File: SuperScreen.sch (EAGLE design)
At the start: 30 parts, among them CN1 AMP FCI 10103594-0001LF, CN2 JSTPH, CN3 1X4-BIG, IC2 MIC5225, Q3 BSS138, U2 MCP73831T-2ACI/OT

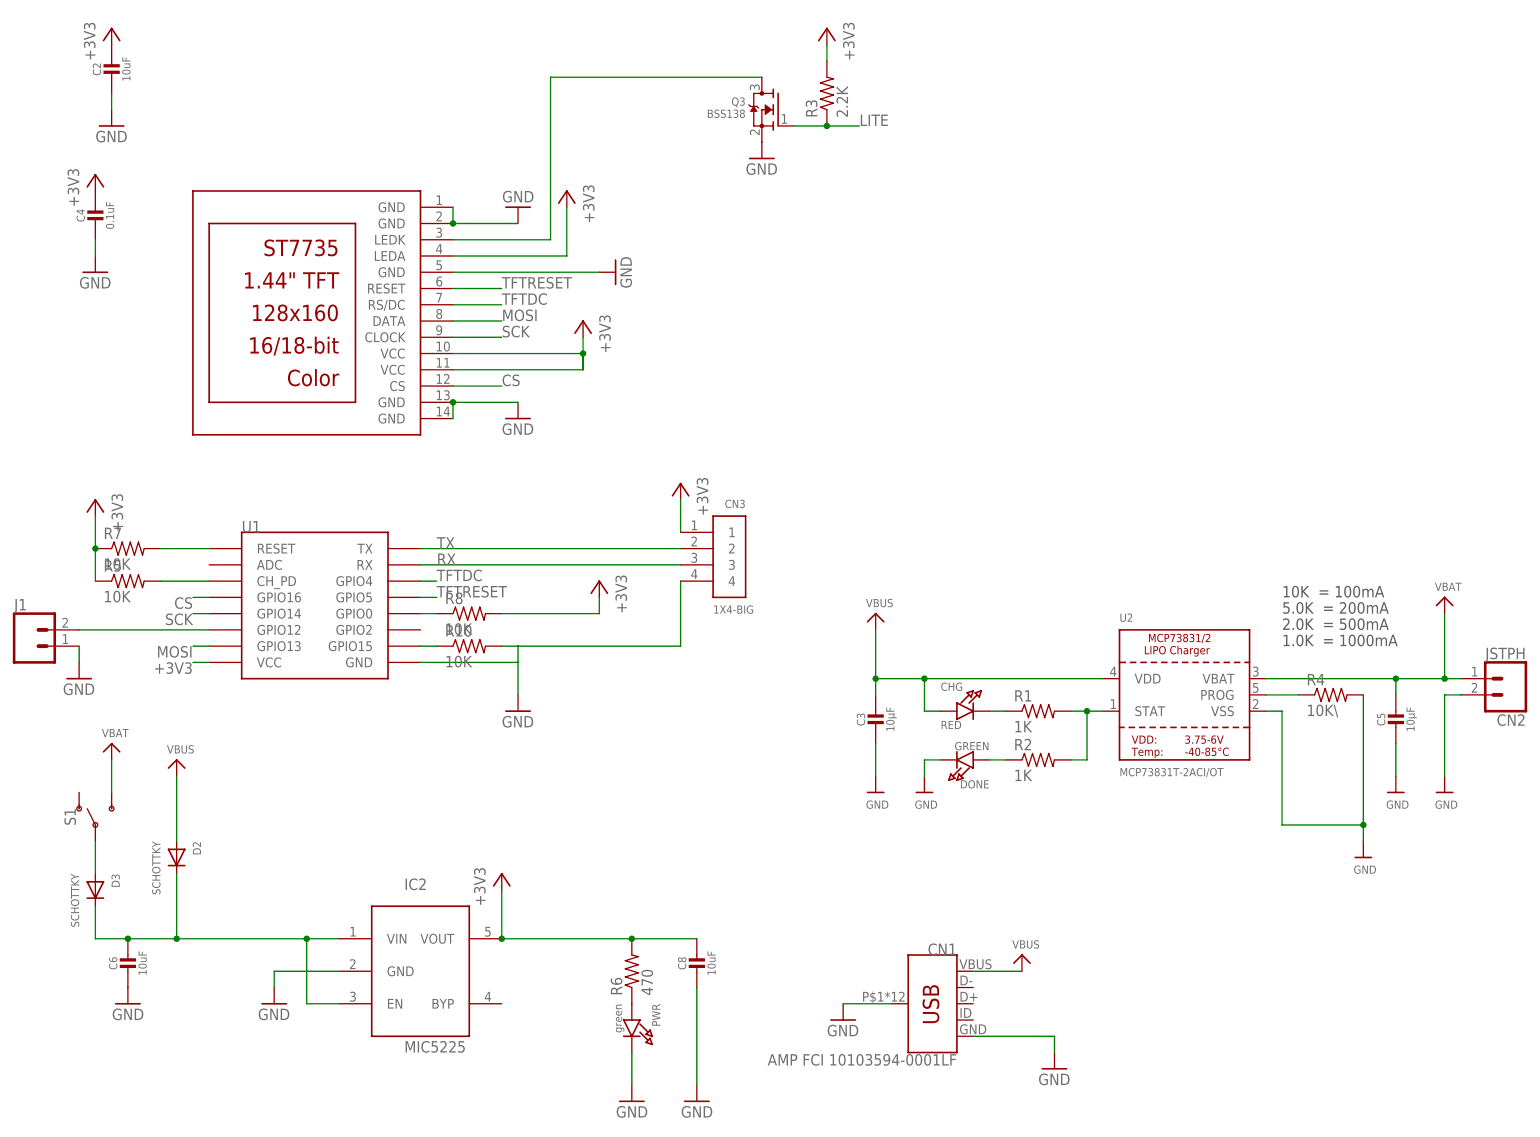
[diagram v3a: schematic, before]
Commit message: Use Adafruit 0805 caps
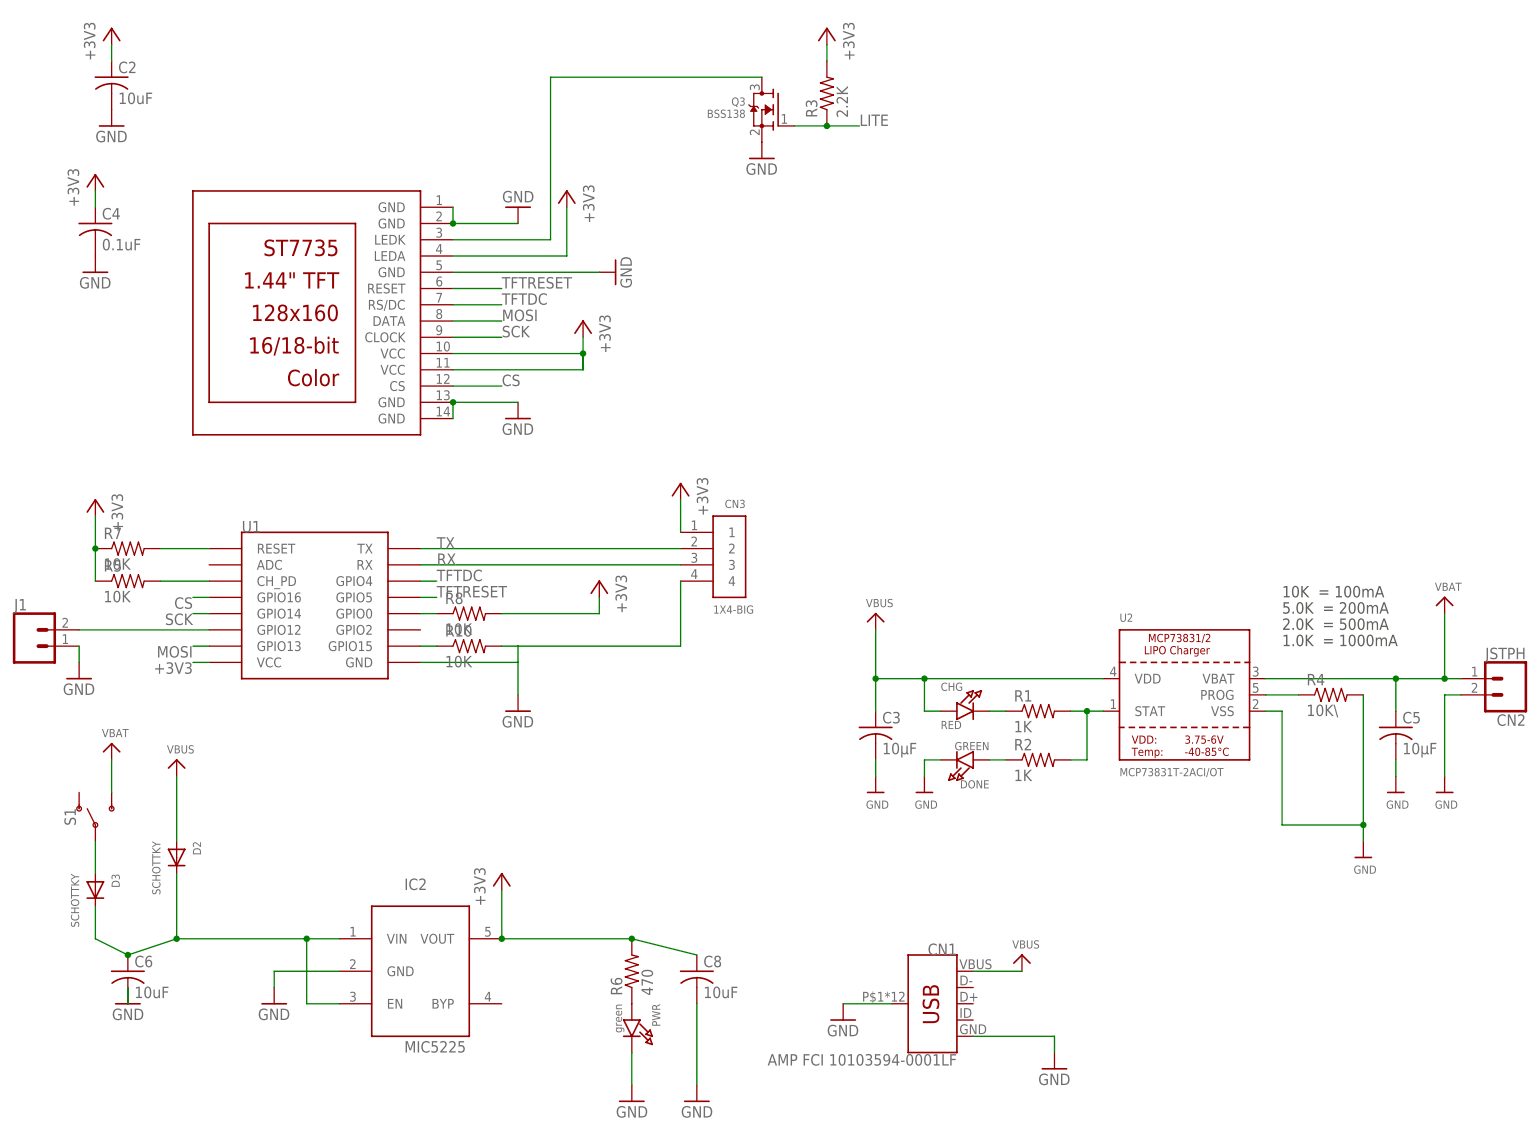
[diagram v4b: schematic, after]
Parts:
- C2, C3, C4, C5, C6, C8: device microbuilder:CAP_CERAMIC0805-NOOUTLINE -> adafruit:C-USC0805
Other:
- moved on the sheet: C2, C3, C4, C5, C6, C8
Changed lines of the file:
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@@
 <part name="+3V3" library="supply1" deviceset="+3V3" device=""/>
 <part name="GND5" library="supply1" deviceset="GND" device=""/>
-<part name="C2" library="microbuilder" deviceset="CAP_CERAMIC" device="0805-NOOUTLINE" value="10uF"/>
+<part name="C2" library="adafruit" library_urn="urn:adsk.eagle:library:420" deviceset="C-US" device="C0805" value="10uF"/>
 <part name="+3V6" library="supply1" deviceset="+3V3" device=""/>
 <part name="GND11" library="supply1" deviceset="GND" device=""/>
-<part name="C4" library="microbuilder" deviceset="CAP_CERAMIC" device="0805-NOOUTLINE" value="0.1uF"/>
+<part name="C4" library="adafruit" library_urn="urn:adsk.eagle:library:420" deviceset="C-US" device="C0805" value="0.1uF"/>
 <part name="+3V8" library="supply1" deviceset="+3V3" device=""/>
 <part name="GND13" library="supply1" deviceset="GND" device=""/>
@@
 <part name="R2" library="adafruit" library_urn="urn:adsk.eagle:library:420" deviceset="R-US_" device="R0805" value="1K"/>
 <part name="CN2" library="SparkFun-Connectors" library_urn="urn:adsk.eagle:library:513" deviceset="CONN_02" device="" package3d_urn="urn:adsk.eagle:package:38039/1" value="JSTPH"/>
-<part name="C3" library="microbuilder" deviceset="CAP_CERAMIC" device="0805-NOOUTLINE" value="10µF"/>
+<part name="C3" library="adafruit" library_urn="urn:adsk.eagle:library:420" deviceset="C-US" device="C0805" value="10µF"/>
 <part name="U$3" library="microbuilder" deviceset="GND" device=""/>
-<part name="C5" library="microbuilder" deviceset="CAP_CERAMIC" device="0805-NOOUTLINE" value="10µF"/>
+<part name="C5" library="adafruit" library_urn="urn:adsk.eagle:library:420" deviceset="C-US" device="C0805" value="10µF"/>
 <part name="U$4" library="microbuilder" deviceset="GND" device=""/>
 <part name="U$5" library="microbuilder" deviceset="GND" device=""/>
@@
 <part name="GND6" library="supply1" deviceset="GND" device=""/>
 <part name="+3V2" library="supply1" deviceset="+3V3" device=""/>
-<part name="C8" library="microbuilder" deviceset="CAP_CERAMIC" device="0805-NOOUTLINE" value="10uF"/>
+<part name="C8" library="adafruit" library_urn="urn:adsk.eagle:library:420" deviceset="C-US" device="C0805" value="10uF"/>
 <part name="PWR" library="microbuilder" deviceset="LED" device="0805_NOOUTLINE" value="green"/>
 <part name="GND7" library="supply1" deviceset="GND" device=""/>
@@
 <part name="U$1" library="microbuilder" deviceset="VBUS" device=""/>
 <part name="U$9" library="microbuilder" deviceset="VBAT" device=""/>
-<part name="C6" library="microbuilder" deviceset="CAP_CERAMIC" device="0805-NOOUTLINE" value="10uF"/>
+<part name="C6" library="adafruit" library_urn="urn:adsk.eagle:library:420" deviceset="C-US" device="C0805" value="10uF"/>
 <part name="GND8" library="supply1" deviceset="GND" device=""/>
 <part name="GND9" library="supply1" deviceset="GND" device=""/>
@@
 <pinref part="C2" gate="G$1" pin="1"/>
 <pinref part="+3V6" gate="G$1" pin="+3V3"/>
+<wire x1="-114.3" y1="43.18" x2="-114.3" y2="40.64" width="0.1524" layer="91"/>
 </segment>
 <segment>
 <pinref part="C4" gate="G$1" pin="1"/>
 <pinref part="+3V8" gate="G$1" pin="+3V3"/>
+<wire x1="-116.84" y1="20.32" x2="-116.84" y2="17.78" width="0.1524" layer="91"/>
 </segment>
 <segment>
@@
 <pinref part="C8" gate="G$1" pin="1"/>
 <pinref part="R6" gate="G$1" pin="2"/>
-<wire x1="-33.02" y1="-96.52" x2="-22.86" y2="-96.52" width="0.1524" layer="91"/>
+<wire x1="-33.02" y1="-96.52" x2="-22.86" y2="-99.06" width="0.1524" layer="91"/>
 <junction x="-33.02" y="-96.52"/>
 </segment>
@@
 <pinref part="C2" gate="G$1" pin="2"/>
 <pinref part="GND11" gate="1" pin="GND"/>
-<wire x1="-114.3" y1="33.02" x2="-114.3" y2="35.56" width="0.1524" layer="91"/>
+<wire x1="-114.3" y1="33.02" x2="-114.3" y2="33.02" width="0.1524" layer="91"/>
 </segment>
 <segment>
 <pinref part="C4" gate="G$1" pin="2"/>
 <pinref part="GND13" gate="1" pin="GND"/>
-<wire x1="-116.84" y1="10.16" x2="-116.84" y2="12.7" width="0.1524" layer="91"/>
+<wire x1="-116.84" y1="10.16" x2="-116.84" y2="10.16" width="0.1524" layer="91"/>
 </segment>
 <segment>
@@
 <pinref part="C3" gate="G$1" pin="2"/>
 <pinref part="U$3" gate="G$1" pin="GND"/>
-<wire x1="5.08" y1="-66.04" x2="5.08" y2="-71.12" width="0.1524" layer="91"/>
+<wire x1="5.08" y1="-68.58" x2="5.08" y2="-71.12" width="0.1524" layer="91"/>
 </segment>
 <segment>
@@
 <pinref part="C5" gate="G$1" pin="2"/>
 <pinref part="U$5" gate="G$1" pin="GND"/>
-<wire x1="86.36" y1="-66.04" x2="86.36" y2="-71.12" width="0.1524" layer="91"/>
+<wire x1="86.36" y1="-68.58" x2="86.36" y2="-71.12" width="0.1524" layer="91"/>
 </segment>
 <segment>
@@
 </segment>
 <segment>
-<wire x1="-22.86" y1="-119.38" x2="-22.86" y2="-104.14" width="0.1524" layer="91"/>
+<wire x1="-22.86" y1="-119.38" x2="-22.86" y2="-106.68" width="0.1524" layer="91"/>
 <pinref part="GND4" gate="1" pin="GND"/>
 <pinref part="C8" gate="G$1" pin="2"/>
@@
 <pinref part="C6" gate="G$1" pin="2"/>
 <pinref part="GND8" gate="1" pin="GND"/>
+<wire x1="-111.76" y1="-104.14" x2="-111.76" y2="-106.68" width="0.1524" layer="91"/>
 </segment>
 <segment>
@@
 <pinref part="C5" gate="G$1" pin="1"/>
 <wire x1="86.36" y1="-55.88" x2="66.04" y2="-55.88" width="0.1524" layer="91"/>
-<wire x1="86.36" y1="-58.42" x2="86.36" y2="-55.88" width="0.1524" layer="91"/>
+<wire x1="86.36" y1="-60.96" x2="86.36" y2="-55.88" width="0.1524" layer="91"/>
 <pinref part="CN2" gate="G$1" pin="1"/>
 <wire x1="86.36" y1="-55.88" x2="93.98" y2="-55.88" width="0.1524" layer="91"/>
@@
 <wire x1="5.08" y1="-55.88" x2="12.7" y2="-55.88" width="0.1524" layer="91"/>
 <wire x1="12.7" y1="-55.88" x2="40.64" y2="-55.88" width="0.1524" layer="91"/>
-<wire x1="5.08" y1="-58.42" x2="5.08" y2="-55.88" width="0.1524" layer="91"/>
+<wire x1="5.08" y1="-60.96" x2="5.08" y2="-55.88" width="0.1524" layer="91"/>
 <junction x="5.08" y="-55.88"/>
 <pinref part="CHG" gate="G$1" pin="A"/>
@@
 <pinref part="D2" gate="G$1" pin="C"/>
 <wire x1="-104.14" y1="-86.36" x2="-104.14" y2="-96.52" width="0.1524" layer="91"/>
-<wire x1="-104.14" y1="-96.52" x2="-111.76" y2="-96.52" width="0.1524" layer="91"/>
+<wire x1="-104.14" y1="-96.52" x2="-111.76" y2="-99.06" width="0.1524" layer="91"/>
 <pinref part="D3" gate="G$1" pin="C"/>
-<wire x1="-111.76" y1="-96.52" x2="-116.84" y2="-96.52" width="0.1524" layer="91"/>
+<wire x1="-111.76" y1="-99.06" x2="-116.84" y2="-96.52" width="0.1524" layer="91"/>
 <wire x1="-116.84" y1="-96.52" x2="-116.84" y2="-91.44" width="0.1524" layer="91"/>
 <wire x1="-83.82" y1="-96.52" x2="-78.74" y2="-96.52" width="0.1524" layer="91"/>
@@
 <junction x="-104.14" y="-96.52"/>
 <pinref part="C6" gate="G$1" pin="1"/>
-<junction x="-111.76" y="-96.52"/>
+<junction x="-111.76" y="-99.06"/>
 <wire x1="-104.14" y1="-96.52" x2="-83.82" y2="-96.52" width="0.1524" layer="91"/>
 </segment>
